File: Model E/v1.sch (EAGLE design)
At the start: 4 parts

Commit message: Added v2
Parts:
- removed C1: (no value), SparkFun-Passives:CAPPTH
- removed SW1: (no value), SparkFun-Connectors:M02PTH
- added JP3: (no value), SparkFun-Connectors:M05X2PTH
- added U$1: ESP-07/12_ESP-12E, ESP-12E:ESP-07/12_ESP-12E
- JP1: device SparkFun-Connectors:M04X2 -> SparkFun-Connectors:M06SILK_FEMALE_PTH
- JP2: device SparkFun-Connectors:M06SILK_FEMALE_PTH -> SparkFun-Connectors:M05X2PTH
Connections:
- removed net GPIO0: JP1.3, SW1.1
- removed net RX: JP1.8, JP2.5
- removed net TX: JP1.1, JP2.4
- new net GPIO14: JP2.5, JP3.5, U$1.P$12
- new net GPIO2: JP3.7, U$1.P$6
- new net N$1: JP1.5, U$1.P$1
- new net N$2: JP1.4, U$1.P$2
- new net N$3: JP1.1, JP1.2, U$1.P$8
- new net N$5: JP2.7, U$1.P$11
- new net N$6: JP2.6, U$1.P$10
- new net SPI_CS: JP2.9, U$1.P$7
- net GND: now also JP3.1; no longer C1.2, JP1.7, SW1.2
- net VCC: now also JP1.3, JP2.2, JP3.3, U$1.P$9; no longer C1.1, JP1.2, JP1.6, JP2.3

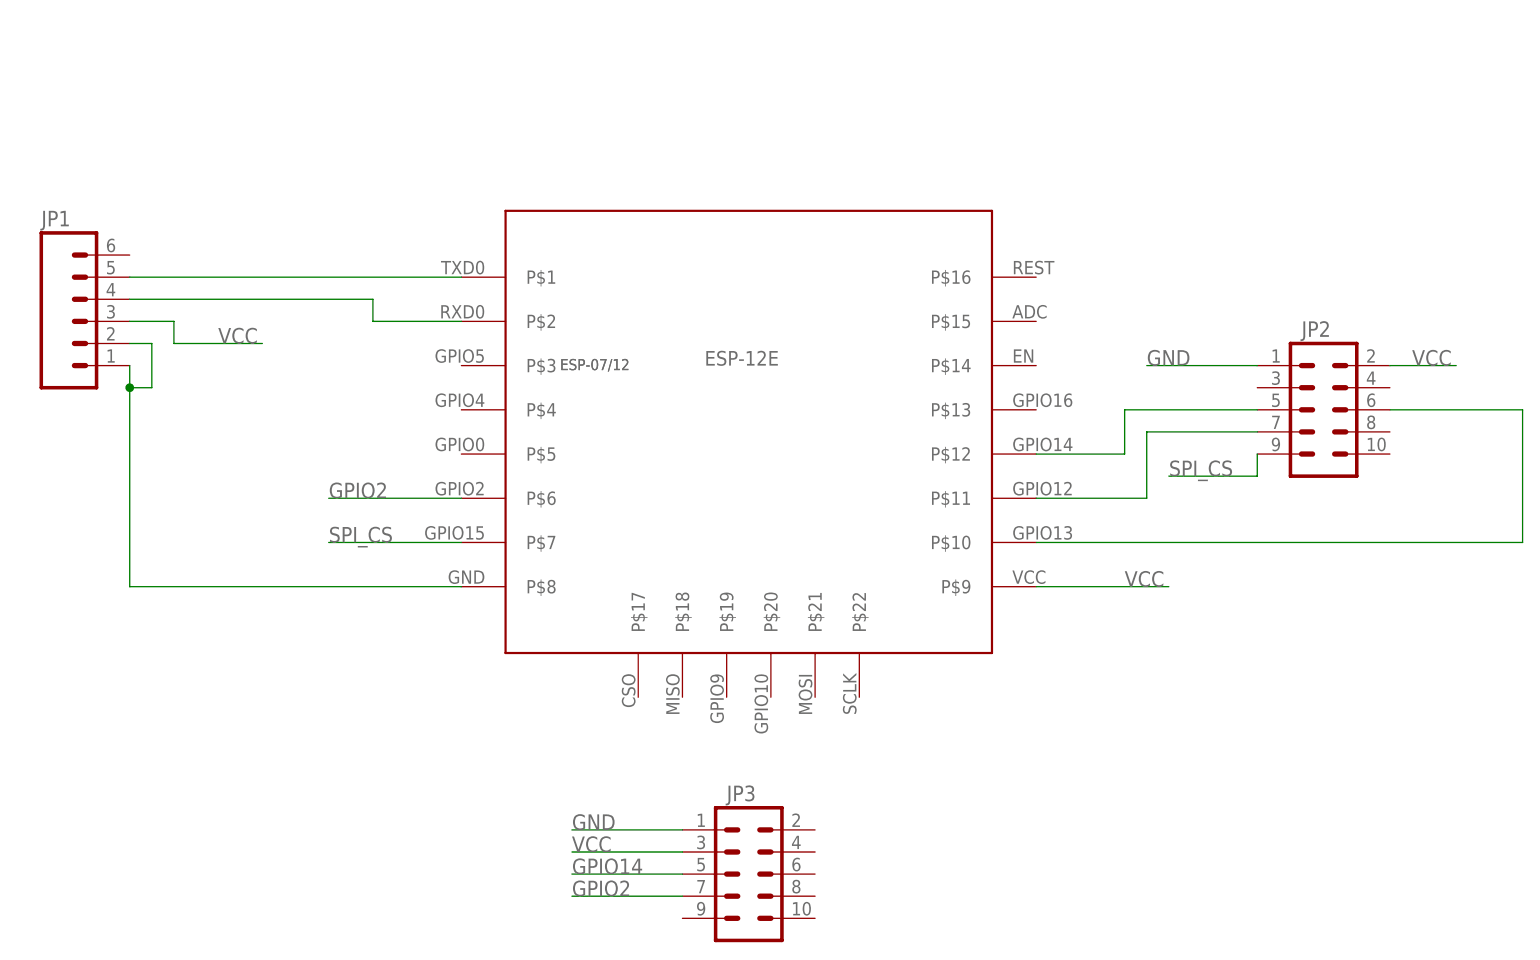
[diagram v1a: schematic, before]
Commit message: added changes before switch to diptrace
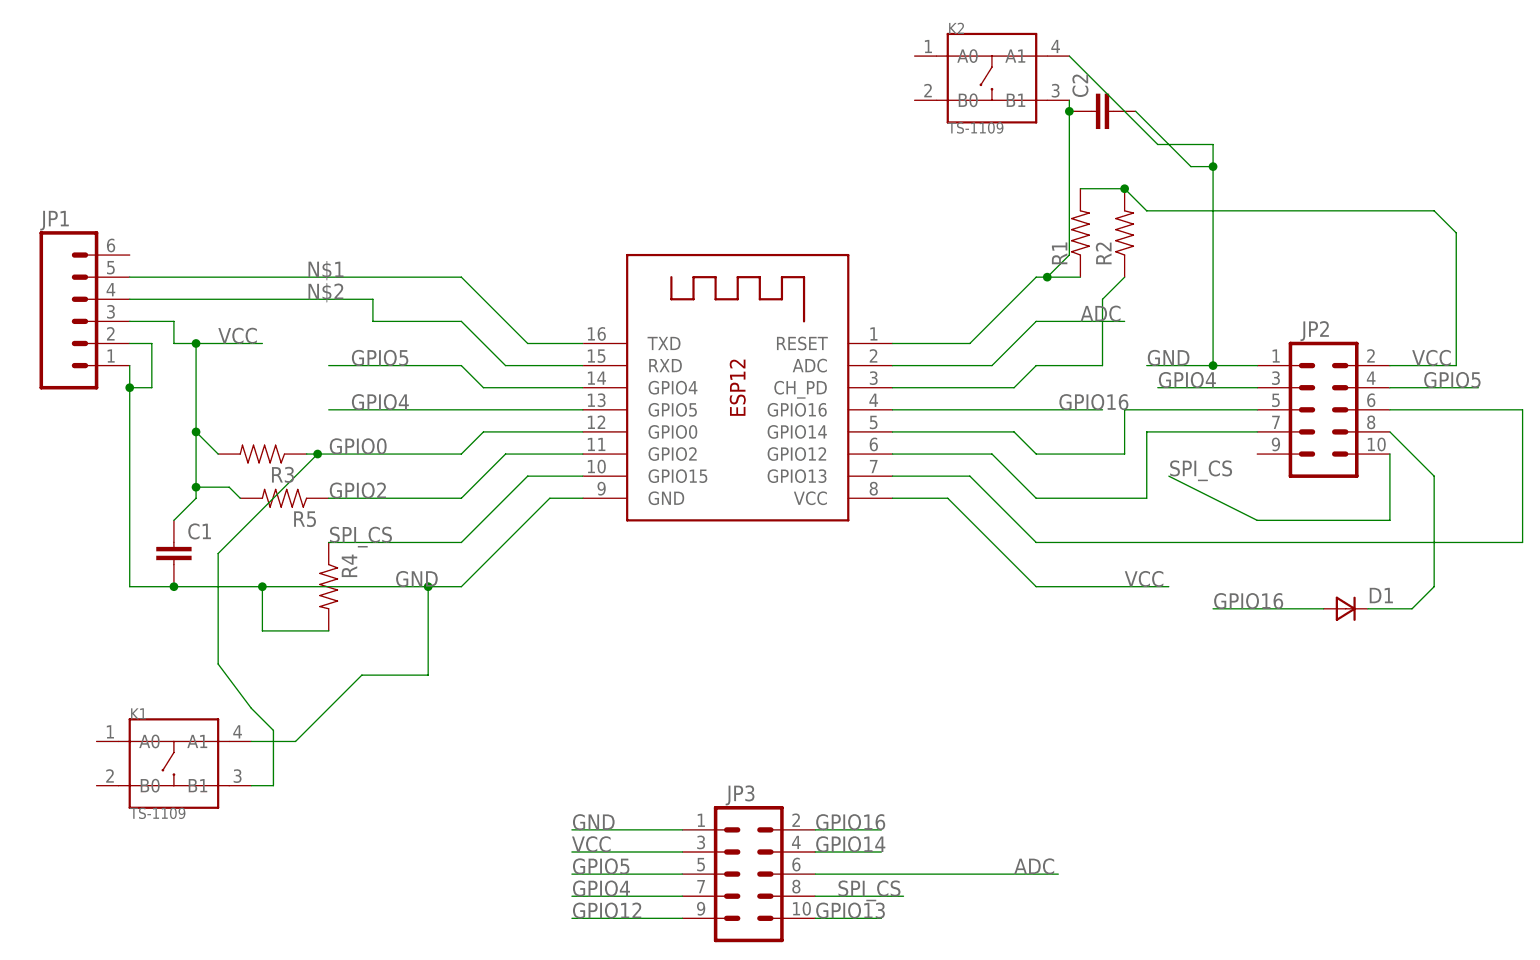
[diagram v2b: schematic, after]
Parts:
- removed U$1: ESP-07/12_ESP-12E, ESP-12E:ESP-07/12_ESP-12E
- added C1, C2: (no value), SparkFun-Capacitors:CAP0805
- added D1: (no value), zetex:DSOD323
- added K1, K2: TS-1109, Seeed-OPL-Button:DIP-BUTTON-4P
- added R1, R2, R3, R4, R5: (no value), SparkFun-Passives:RESISTOR0805-RES
- added X1: (no value), adafruit:ESP-12
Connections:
- removed net N$3: JP1.1, JP1.2, U$1.P$8
- new net ADC: JP3.6, X1.ADC
- new net GPIO0: K1.B1, R3.1, X1.GPIO0
- new net GPIO12: JP3.9
- new net GPIO13: JP3.10
- new net GPIO16: D1.A, JP3.2, X1.GPIO16
- new net GPIO4: JP2.3, JP3.7, X1.GPIO5
- new net GPIO5: JP2.4, JP3.5, X1.GPIO4
- new net N$10: C2.1, K2.B1, R1.1, X1.RESET
- new net N$11: R2.1, X1.CH_PD
- new net N$9: D1.C, JP2.8
- net GND: now also C1.2, C2.2, JP1.1, JP1.2, K1.A1, K2.A1, R4.2, X1.GND
- net GPIO14: now also JP3.4, X1.GPIO14; no longer JP3.5, U$1.P$12
- net GPIO2: now also R5.1, X1.GPIO2; no longer JP3.7, U$1.P$6
- net N$1: now also X1.TXD; no longer U$1.P$1
- net N$2: now also X1.RXD; no longer U$1.P$2
- net N$5: now also X1.GPIO12; no longer U$1.P$11
- net N$6: now also X1.GPIO13; no longer U$1.P$10
- net SPI_CS: now also JP2.10, JP3.8, R4.1, X1.GPIO15; no longer JP2.9, U$1.P$7
- net VCC: now also C1.1, R1.2, R2.2, R3.2, R5.2, X1.VCC; no longer U$1.P$9
